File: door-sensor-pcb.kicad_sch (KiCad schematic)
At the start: 44 parts, among them J1 peripherals, J2 RPi, J3 RPi, J4 DC2DC, J5 DC2DC, Q1 BC546, Q2 BC546, Q3 BC546, Q4 BC546, Q5 BC546, Q6 BC546, Q7 BC546, Q8 BC546, Q9 BC546

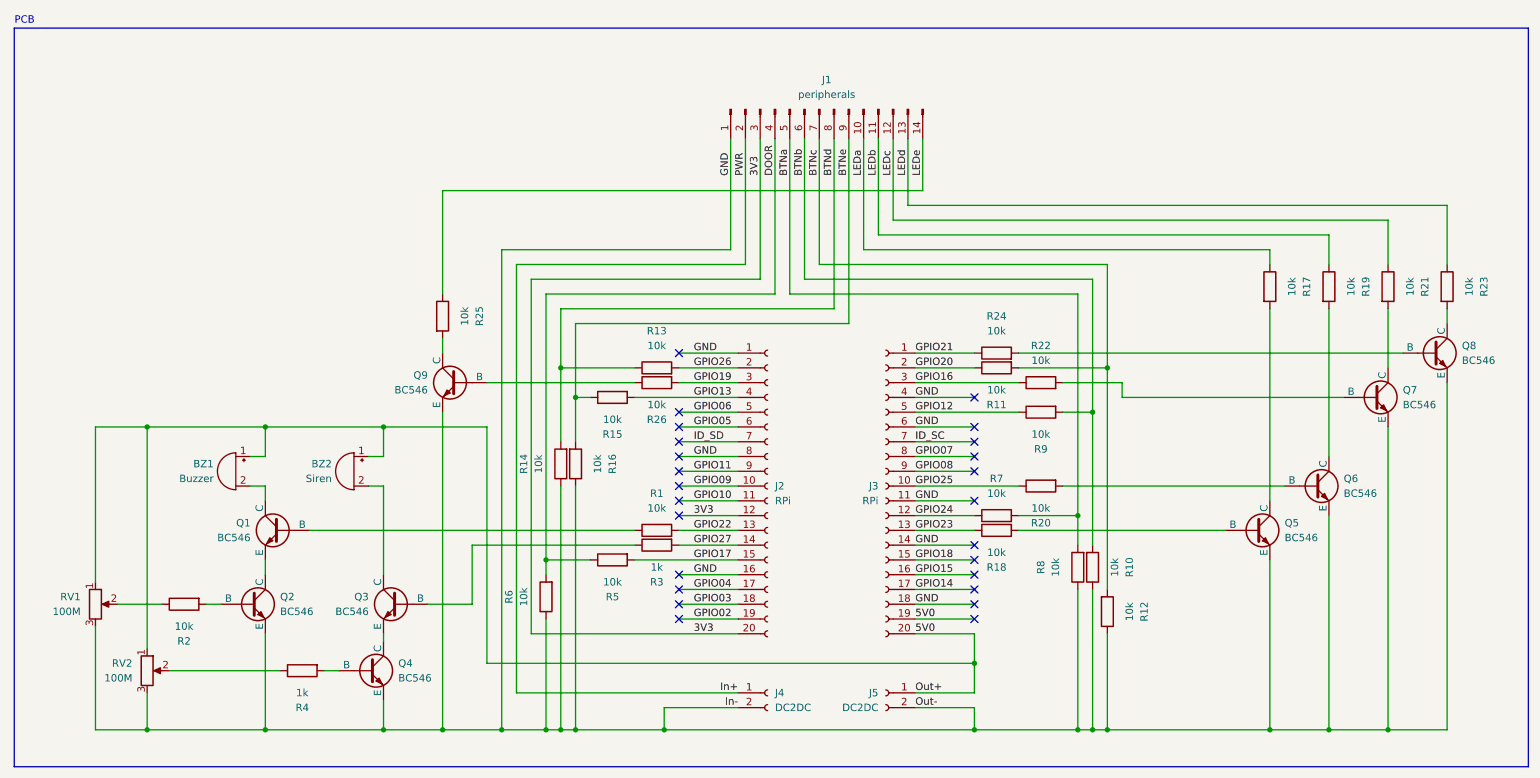
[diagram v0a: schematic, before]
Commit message: Door sensor documentation update
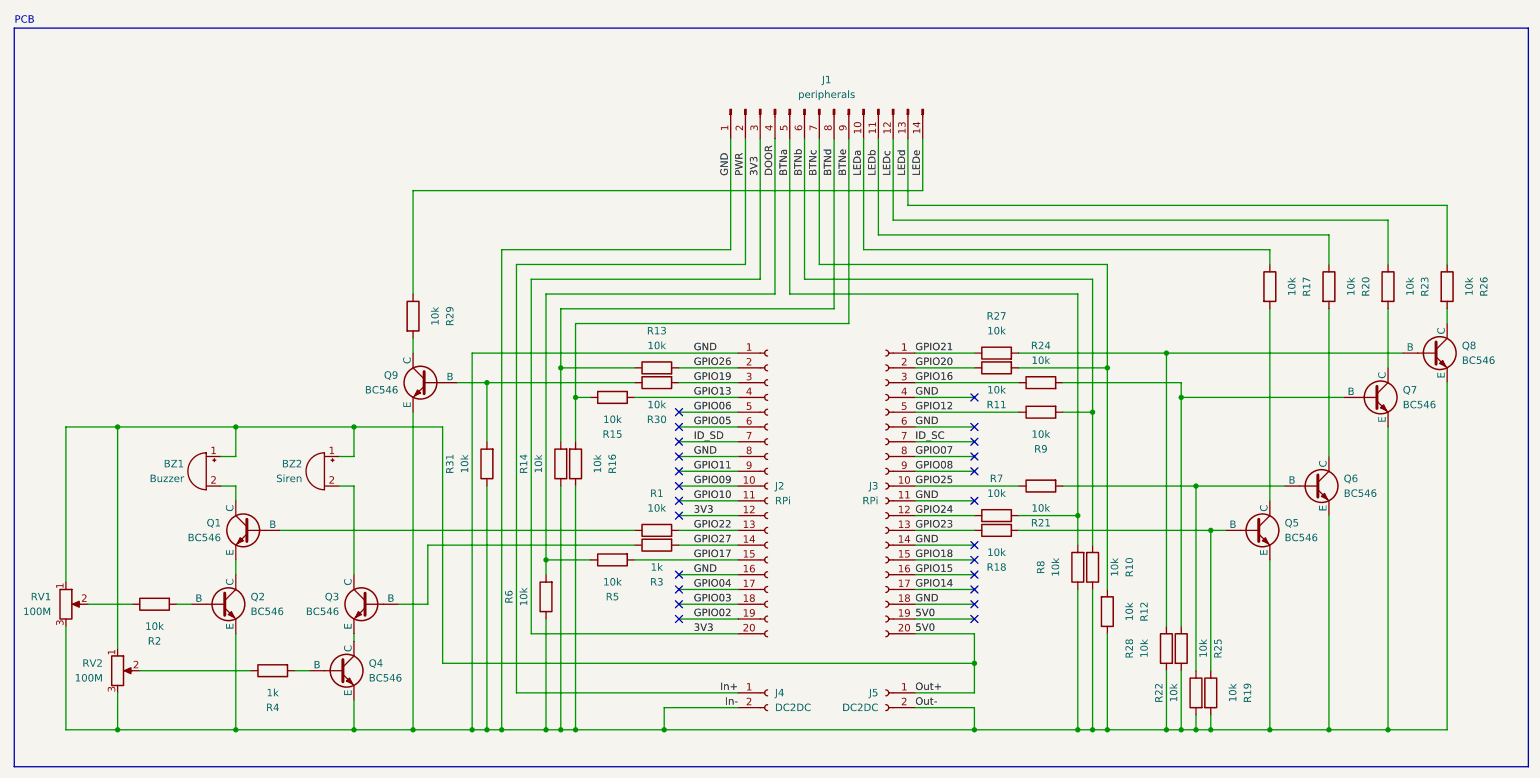
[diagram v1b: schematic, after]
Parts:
- added R19, R22, R25, R28, R31: 10k, symbol Device:R
- renumbered R19 to R20, R20 to R21, R21 to R23, R22 to R24, R23 to R26, R24 to R27, R25 to R29, R26 to R30
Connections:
- net GND: now also R19.2, R22.2, R25.2, R28.2, R31.1
- net at Q9.2 (B), R30.1: now also R31.2
- net at Q7.2 (B), R24.2: now also R25.1
- net at Q8.2 (B), R27.2: now also R28.1
- net at Q5.2 (B), R18.2: now also R19.1
- net at Q6.2 (B), R21.2: now also R22.1
- no-connect marks 25 -> 24
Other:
- moved on the sheet: BZ1, BZ2, Q1, Q2, Q3, Q4, Q9, R2, R29, R4, RV1, RV2
